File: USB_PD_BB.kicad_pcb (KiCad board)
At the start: 2 copper layers, 70 x 50 mm, 11 parts, among them CN1 53375-0410, CN2 53375-1010, CN3 53375-0210, CN4 53375-0310, CN5 53375-0510, U1 AM26C31, U2 TLP2168, U3 TLP290-4, U4 TLP290

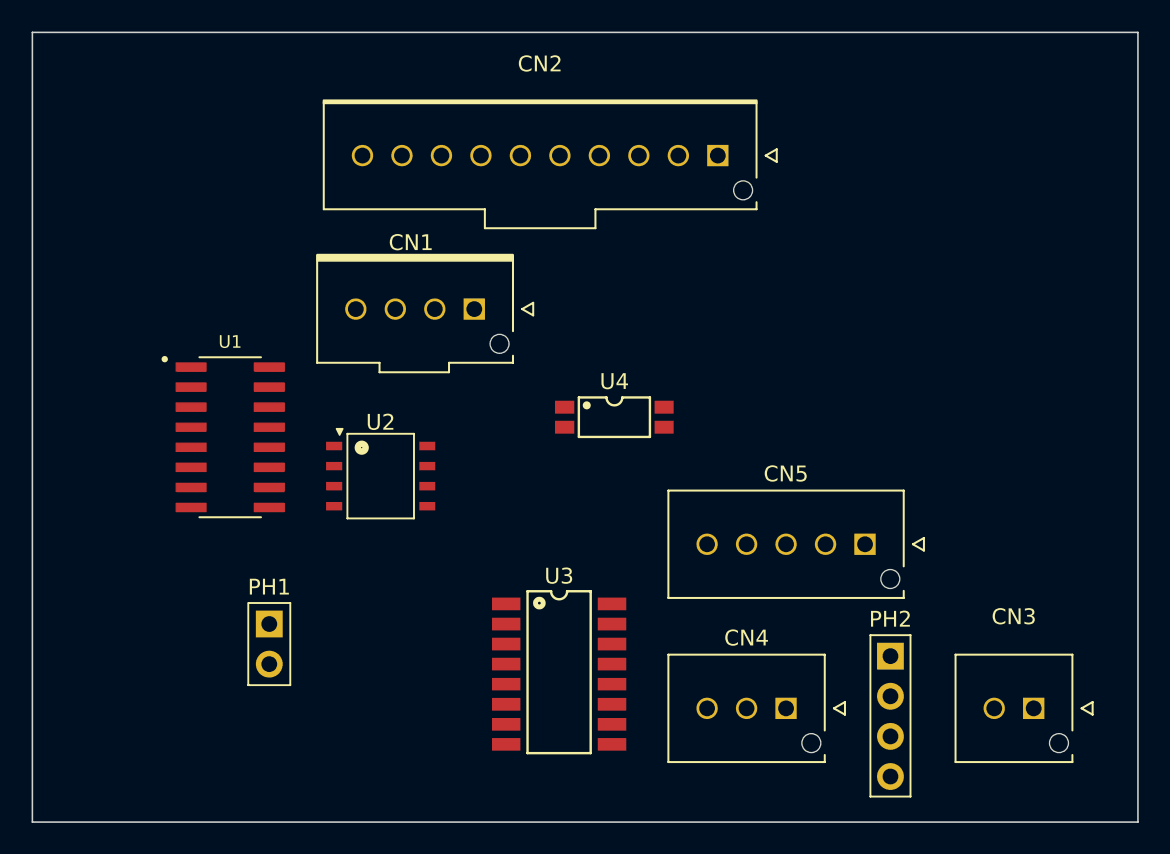
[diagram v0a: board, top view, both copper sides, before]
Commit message: add USB-PD
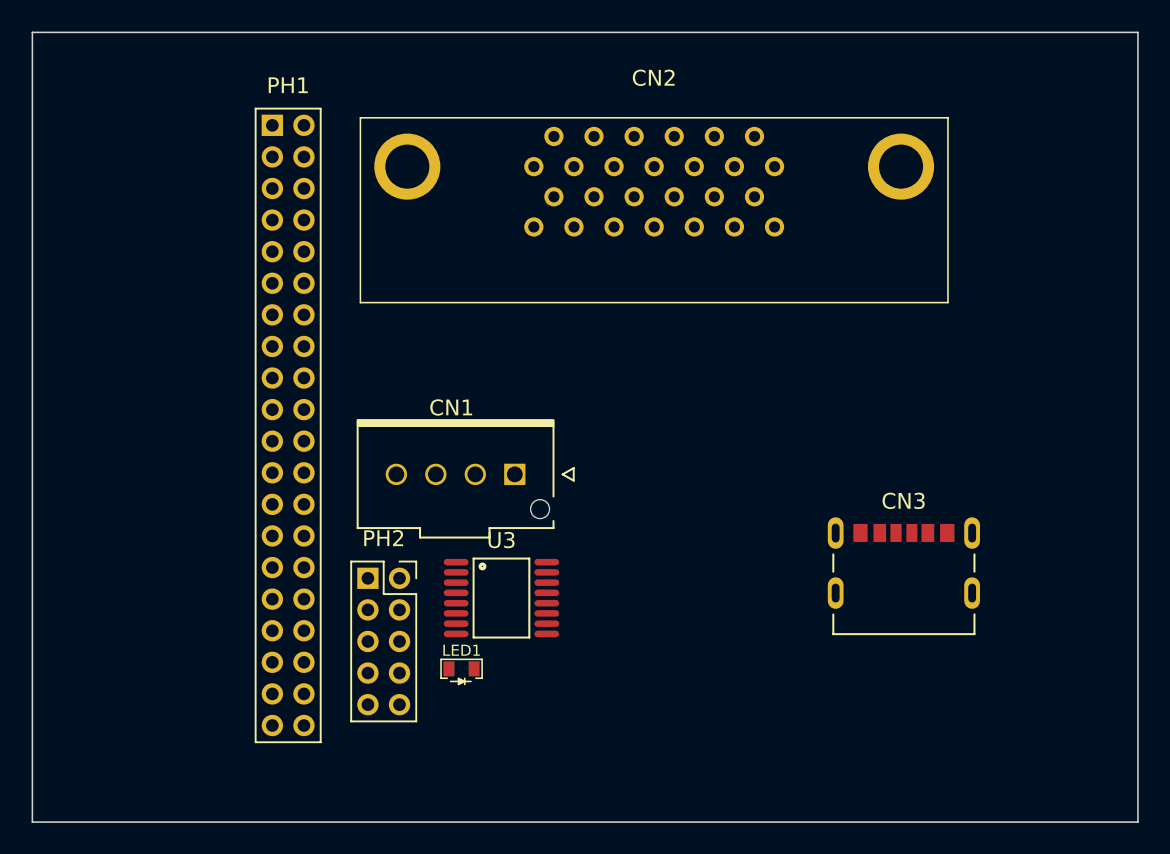
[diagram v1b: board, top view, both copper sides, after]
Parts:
- removed CN4: 53375-0310, Connector:53375-0310
- removed CN5: 53375-0510, Connector:53375-0510
- removed U1: AM26C31, Interface:AM26C31
- removed U2: TLP2168, Interface:TLP2168
- removed U4: TLP290, Interface:TLP290
- added LED1: Value, Basic:LED1608mRED, F.Cu at (127.2, 105.3)
- CN2: value 53375-1010 -> 10126-5212PC; footprint Connector:53375-1010 -> Connector:10126-5212PC
- CN3: value 53375-0210 -> UJC-HP-3-SMT-TR; footprint Connector:53375-0210 -> Connector:UJC-HP-3-SMT-TR
- PH1: value ~ -> PinSocket2mm_2x20; footprint PinHeader:PinHeader2x1 -> PinSocket:PinSocket2mm_2x20
- PH2: value PinHeader4x1 -> PinSocket2mm_2x5; footprint PinHeader:PinHeader4x1 -> PinSocket:PinSocket2mm_2x5
- U3: value TLP290-4 -> IP2721D; footprint Interface:TLP290-4 -> IC:IP2721D
- moved PH1 32.9 mm to (117.2, 70.9)
- moved PH2 32.3 mm to (123.2, 99.6)
- moved CN3 13.1 mm to (155.2, 96.7)
- moved CN1 10.8 mm to (126.8, 93.0)
- moved CN2 7.42 mm to (139.4, 74.5)
- moved U3 6.05 mm to (129.7, 100.8)

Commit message: add FET ans Switch
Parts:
- removed CN2: 10126-5212PC, Connector:10126-5212PC
- removed CN3: UJC-HP-3-SMT-TR, Connector:UJC-HP-3-SMT-TR
- removed LED1: Value, Basic:LED1608mRED
- removed PH2: PinSocket2mm_2x5, PinSocket:PinSocket2mm_2x5
- added C1: 1uF/50V, Basic:CAP1608m, F.Cu at (118.0, 98.0)
- added C2: Value, Basic:CAP1608m, F.Cu at (113.3, 98.0)
- added R1: 5.1k, Basic:REG1608m, F.Cu at (124.0, 85.0)
- added R2: 5.1k, Basic:REG1608m, F.Cu at (124.0, 82.0)
- added R3: 100k, Basic:REG1608m, F.Cu at (122.2, 96.0)
- added R4: 100k, Basic:REG1608m, F.Cu at (122.0, 98.0)
- added SW1: 2MS1-T1-B4-VS2-S-E, Switch:2MS1-T1-B4-VS2-Q-E-S, F.Cu at (130.0, 88.2)
- added TR1: AO3400A, Discrete:AO3400A, F.Cu at (122.0, 91.0)
- CN1: value 53375-0410 -> UJC-HP-3-SMT-TR; footprint Connector:53375-0410 -> Connector:UJC-HP-3-SMT-TR
- PH1: value PinSocket2mm_2x20 -> PinHeader3x2; footprint PinSocket:PinSocket2mm_2x20 -> PinHeader:PinHeader3x2; moved to B.Cu
- moved PH1 30.8 mm to (132.5, 97.5), turned to 90 degrees
- moved U3 15.3 mm to (116.0, 94.0)
- moved CN1 12.5 mm to (116.0, 86.7), turned to 180 degrees
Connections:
- U3 pad 1: unconnected-(U3-VBUSG-Pad1) -> Net-(U3-VBUSG)
- U3 pad 11: unconnected-(U3-SEL-Pad11) -> /SEL
- U3 pad 12: unconnected-(U3-CC2-Pad12) -> /CC2
- U3 pad 13: unconnected-(U3-CC1-Pad13) -> /CC1
- U3 pad 16: unconnected-(U3-VBUS-Pad16) -> /Vout
- U3 pad 2: unconnected-(U3-VIN-Pad2) -> Vin
- U3 pad 5: unconnected-(U3-GND-Pad5) -> GND
- U3 pad 6: unconnected-(U3-SELP-Pad6) -> /SELP
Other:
- board size 70 x 50 mm -> 25 x 20 mm

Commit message: rough artwork.
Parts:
- added JP1: ~, Jumper:SolderJumperSel, F.Cu at (114.4, 91.2)
- added JP2: ~, Jumper:SolderJumperSel, F.Cu at (111.8, 91.2)
- R1, R2, R3, R4, U3: moved to B.Cu
- moved C2 19.2 mm to (119.0, 79.7), turned to 90 degrees
- moved C1 18.7 mm to (121.5, 79.7), turned to 90 degrees
- moved R1 11.8 mm to (112.5, 82.5), turned to 180 degrees
- moved R2 11.8 mm to (112.5, 84.5), turned to 180 degrees
- moved R3 11.5 mm to (111.8, 91.2), turned to 90 degrees
- moved U3 10.9 mm to (119.0, 83.5), turned to 180 degrees
- moved R4 10.2 mm to (114.4, 91.2), turned to 90 degrees
- moved PH1 7.77 mm to (133.2, 89.8), turned to -90 degrees
- moved TR1 7.76 mm to (120.0, 83.5), turned to 180 degrees
- moved SW1 3.88 mm to (126.8, 86.0)
- moved CN1 3.21 mm to (115.7, 83.5), turned to -90 degrees
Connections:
- PH1 pad 1: unconnected-(PH1-Pad1) -> Net-(PH1-Pad1)
- PH1 pad 2: unconnected-(PH1-Pad2) -> GND
- PH1 pad 3: unconnected-(PH1-Pad3) -> Net-(PH1-Pad1)
- PH1 pad 4: unconnected-(PH1-Pad4) -> GND
- PH1 pad 5: unconnected-(PH1-Pad5) -> Net-(PH1-Pad1)
- PH1 pad 6: unconnected-(PH1-Pad6) -> GND
- R3 pad 2: /SEL -> Net-(JP2-Pad2)
- R4 pad 2: /SELP -> Net-(JP1-Pad2)
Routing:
- net /SELP: track 0.00 -> 12.1 mm, vias 0 -> 1
- net /SEL: track 0.00 -> 9.69 mm, vias 0 -> 1
- net /CC2: track 0.00 -> 4.31 mm, vias 0 -> 1
- net /CC1: track 0.00 -> 4.31 mm, vias 0 -> 1
- net Vin: track 0.00 -> 2.60 mm
- net Net-(JP2-Pad2): track 0.00 -> 2.20 mm, vias 0 -> 1
- net Net-(JP1-Pad2): track 0.00 -> 2.20 mm, vias 0 -> 1
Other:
- board size 25 x 20 mm -> 30 x 16 mm
- board text added: "12V"
- board text added: "15V"
- board text added: "20V"
- board text added: "5V"
- board text added: "9V"
- board text added: "GND"
- board text added: "OFF"
- board text added: "ON"
- board text added: "Vout"
